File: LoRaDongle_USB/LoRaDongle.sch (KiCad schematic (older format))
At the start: 7 parts

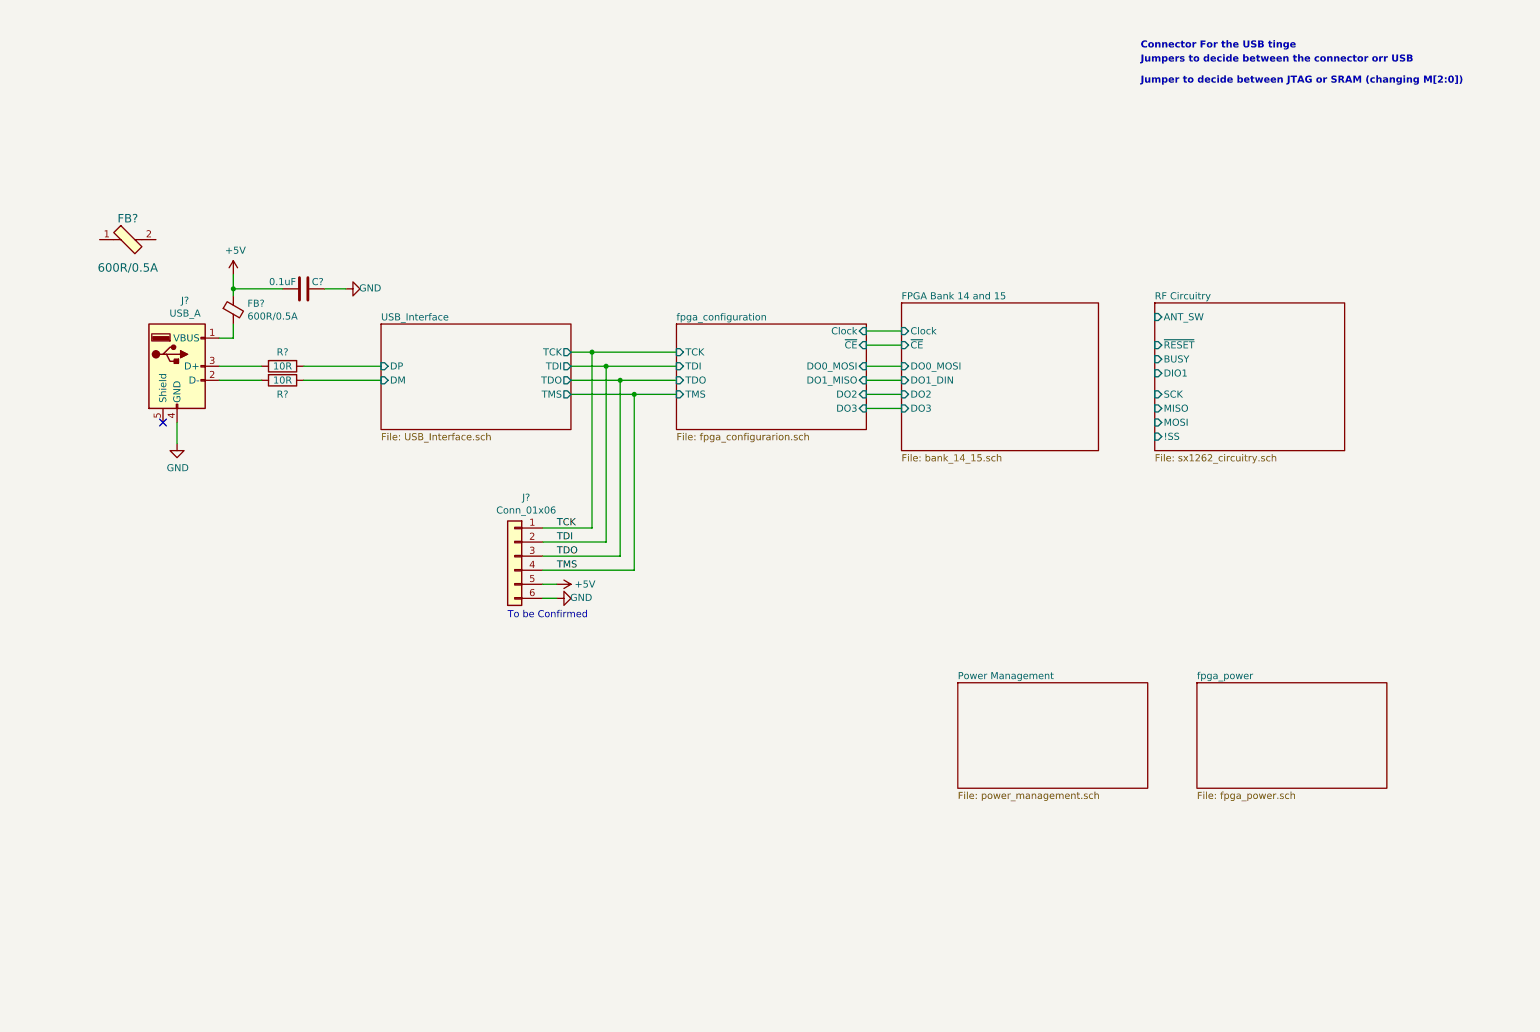
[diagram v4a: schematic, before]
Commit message: updated with dip switch
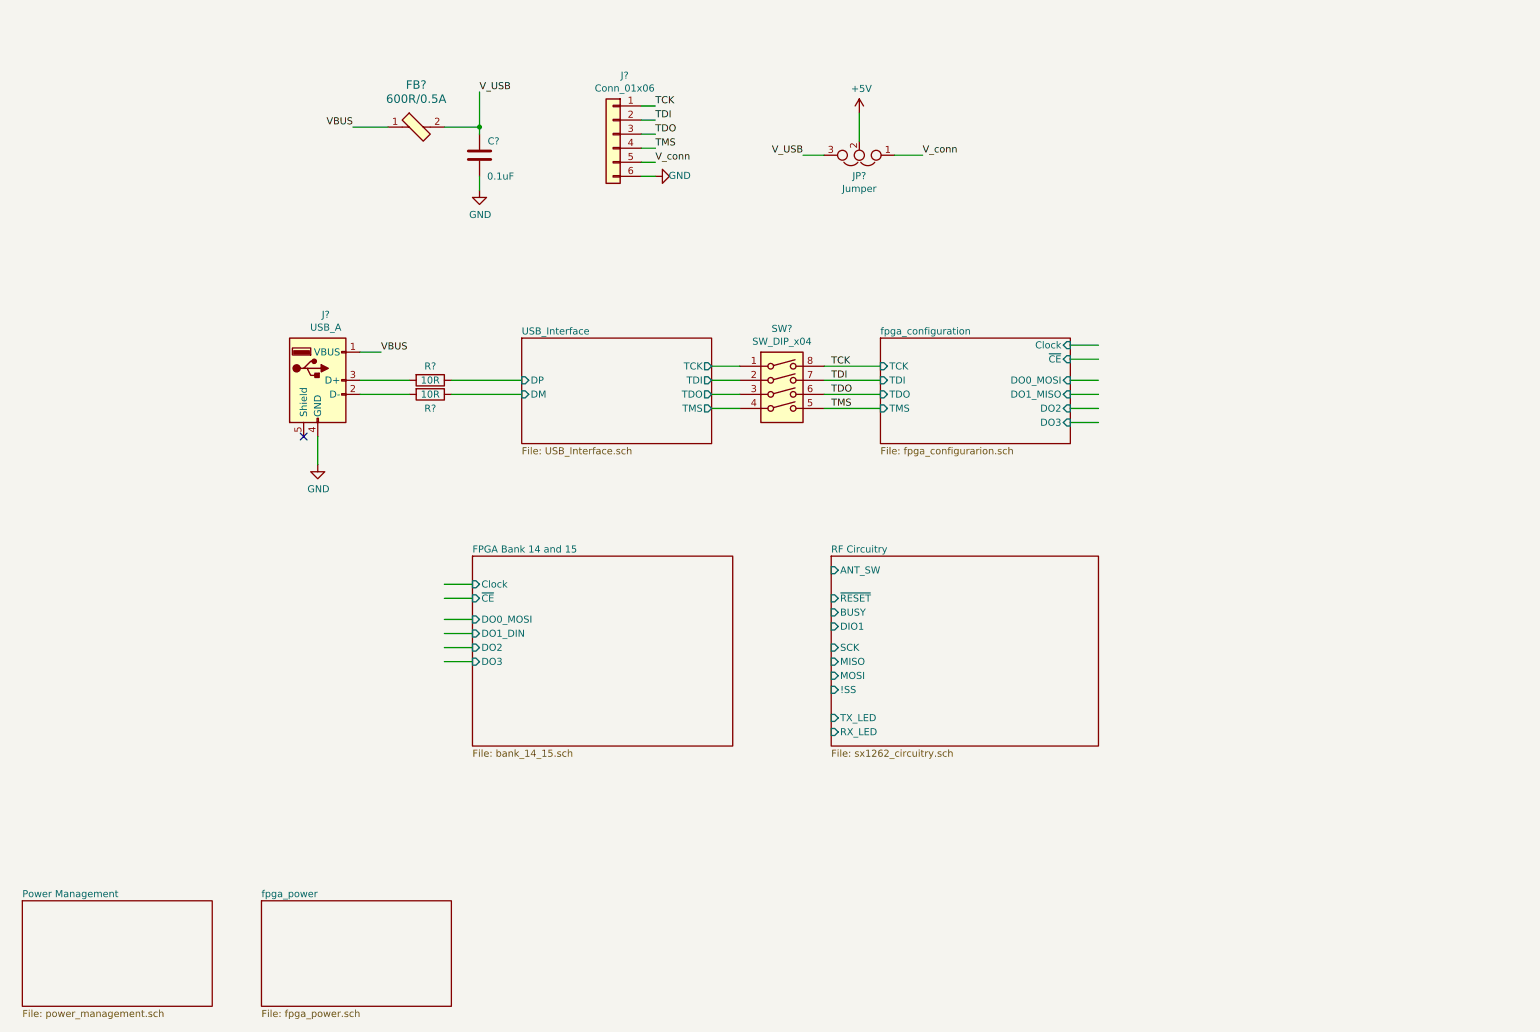
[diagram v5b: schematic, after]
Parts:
- removed FB?: 600R/0.5A, digikey-footprints:0603, symbol Device:Ferrite_Bead_Small
- added JP?: Jumper, symbol Device:Jumper_NC_Dual
- added SW?: SW_DIP_x04, symbol Switch:SW_DIP_x04
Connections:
- net labels added: VBUS, V_USB, V_conn
- wire segments 35 -> 40
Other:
- note removed: "Connector For the USB tinge"
- note removed: "Jumper to decide between JTAG or SRAM (changing M[2:0])"
- note removed: "Jumpers to decide between the connector orr USB"
- note removed: "To be Confirmed"
- moved on the sheet: C?, FB?, J?, R?
